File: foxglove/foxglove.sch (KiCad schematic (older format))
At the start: 23 parts, among them J1 NEIGHBOR1, J2 NEIGHBOR2, J7 BONUS_ROW, U10 iCE40HX4K

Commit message: Added iCE40-HX8K-CT256 to schematic, began signal routing.
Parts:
- removed C? (x2): 100nF, symbol Device:C
- removed C? (x2): 10uF, symbol Device:C
- removed J?: Conn_01x02, symbol Connector_Generic:Conn_01x02
- removed R? (x2): 100, symbol Device:R
- removed R? (x3): 10k, symbol Device:R
- removed U10: iCE40HX4K, gsg-modules:LQFP144, symbol gsg-symbols:iCE40HX4K
- removed U? (x5): ICE40HX8K-BG121, Package_BGA:BGA-121_9.0x9.0mm_Layout11x11_P0.8mm_Ball0.4mm_Pad0.35mm_NSMD, symbol FPGA_Lattice:ICE40HX8K-BG121
- added C? (x2): 10uF, symbol Device:C
- added C? (x2): 100nF, symbol Device:C
- added R? (x2): 100, symbol Device:R
- added R? (x3): 10k, symbol Device:R
- added R?: ???, symbol Device:R
- added U1: ICE40HX8K-CT256, BGA256C80P16X16_1400X1400X170, symbol gsg-symbols:ICE40HX8K-CT256
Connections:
- net labels added: J1.03, J1.04, J1.05, J1.06, J1.07, J1.08, J1.09, J1.10, J1.11, J1.12, J1.13, J1.14, J1.15, J1.16, J1.17, J1.18, J1.19, J1.20, J1.21, J1.22, J1.23, J1.24, J1.25, J1.26, J1.27, J1.28, J1.29, J1.30, J1.31, J1.32, J1.33, J1.34, J1.35, J1.36
- net labels removed: SPI_MISO, SPI_MOSI, SPI_SCK, SPI_SSEL
- wire segments 96 -> 57
- no-connect marks 65 -> 59
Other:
- note added: "add picture?\n"
- note removed: "FPGA should be able to reroute all GreatFET pins"
- note removed: "P0_0"
- note removed: "P0_1"
- note removed: "P1_0"
- note removed: "P1_10"
- note removed: "P1_11"
- note removed: "P1_12"
- note removed: "P1_13"
- note removed: "P1_14"
- note removed: "P1_15"
- note removed: "P1_16"
- note removed: "P1_7"
- note removed: "P1_8"
- note removed: "P1_9"
- note removed: "P5_0"
- note removed: "P5_1"
- note removed: "don't connect PLL ground\nto board ground"
- moved on the sheet: J1, J2, J7, MH1, MH2, MH3, MH4

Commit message: Foxglove: Routed signals to FPGA and set up bank A multiplexors
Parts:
- added C10, C11, C12, C5, C6, C7: 1uF, gsg-modules:0402, symbol Device:C
- added C8, C9: 0.1uF, gsg-modules:0402, symbol Device:C
- added J3, J4: Conn_02x05_Odd_Even, gsg-modules:HEADER-2x5, symbol Connector_Generic:Conn_02x05_Odd_Even
- added J5: Conn_01x02_Female, gsg-modules:HEADER-1x2, symbol Connector_Generic:Conn_01x02
- added R10, R15, R7: 10k, gsg-modules:0402, symbol Device:R
- added R11, R14: 165k, gsg-modules:0402, symbol Device:R
- added R12, R16: 20k, gsg-modules:0402, symbol Device:R
- added R13, R8: 217k, gsg-modules:0402, symbol Device:R
- added R9: 5k, gsg-modules:0402, symbol Device:R
- added U2: TLV711, Package_SON:WSON-6_1.5x1.5mm_P0.5mm, symbol gsg-symbols:TLV711
- added U3: MC4558CPT, Package_SO:TSSOP-8_4.4x3mm_P0.65mm, symbol gsg-symbols:MC4558CPT
- added U4: 74LVC1G3157, gsg-modules:SOT363, symbol gsg-symbols:74LVC1G3157
- added U5: LM339, Package_SO:SOIC-14_3.9x8.7mm_P1.27mm, symbol gsg-symbols:LM339
- added U6: ADP225, Package_CSP:LFCSP-8_2x2mm_P0.5mm, symbol gsg-symbols:ADP225
- added U7: DAC084S085, Package_SON:WSON-8-1EP_3x3mm_P0.5mm_EP1.6x2.0mm, symbol gsg-symbols:DAC084S085
- added U8: 74AHC1G04, Package_TO_SOT_SMD:SOT-886, symbol gsg-symbols:74AHC1G04
- C1, C2, C3, C4: renamed from C?; footprint (none) -> gsg-modules:0402
- R1, R2, R3, R4, R5, R6: renamed from R?; footprint (none) -> gsg-modules:0402
- U1: footprint BGA256C80P16X16_1400X1400X170 -> gsg-modules:BGA256C80P16X16_1400X1400X170
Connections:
- net +1V2: now also C7.1, U2.6 (OUT1)
- net +2V5: now also C6.1, U2.5 (OUT2)
- net +5V: now also C11.1, C5.1, C8.1, C9.2, R15.1, U2.1 (EN1), U2.2 (IN), U2.3 (EN2), U3.8 (VCC+), U5.3 (VCC), U6.6 (VIN), U7.7 (VREFIN)
- net GND: now also C10.2, C11.2, C12.2, C5.2, C6.2, C7.2, C8.2, C9.1, J3.10 (Pin_10), J4.10 (Pin_10), J5.1 (Pin_1), R10.1, R12.1, R16.2, R7.2, U2.4 (GND), U3.4 (VCC-), U4.2 (GND), U5.12 (GND), U6.3 (GND), U7.6 (GND), U8.3 (GND)
- net J1.03: now also U1.P13 (IOB_104_CBSEL1); no longer U1.R16 (IOB_102)
- net J1.04: now also U1.K11 (IOB_103_CBSEL0); no longer U1.M12 (IOB_101)
- net J1.05: now also U1.R16 (IOB_102); no longer U1.T16 (IOB_100)
- net J1.06: now also U1.M12 (IOB_101); no longer U1.L11 (IOB_99)
- net J1.07: now also U1.T16 (IOB_100)
- net J1.08: now also U1.L11 (IOB_99)
- net J1.09: now also U1.N12 (IOB_98)
- net J1.10: now also U1.T13 (IOB_94)
- net J1.11: now also U1.M11 (IOB_93)
- net J1.12: now also U1.T14 (IOB_92)
- net J1.13: now also U1.T15 (IOB_91)
- net J1.14: now also U1.T11 (IOB_89)
- net J1.15: now also U1.T10 (IOB_88)
- net J1.16: now also U1.N10 (IOB_87)
- net J1.17: now also U1.P10 (IOB_86)
- net J1.18: now also U1.L10 (IOB_85)
- net J1.19: now also U1.R10 (IOB_84)
- net J1.20: now also U1.P9 (IOB_83)
- net J1.21: now also U1.K9 (IOB_82_GBIN4)
- net J1.22: now also U1.R9 (IOB_81_GBIN5)
- net J1.23: now also U1.M9 (IOB_80)
- net J1.24: now also U1.T9 (IOB_79)
- net J1.25: now also U1.N9 (IOB_78)
- net J1.26: now also U1.P7 (IOB_77)
- net J1.27: now also U1.T8 (IOB_76)
- net J1.28: now also U1.T7 (IOB_75)
- net J1.29: now also U1.L9 (IOB_74)
- net J1.30: now also U1.T6 (IOB_73)
- net J1.32: now also U1.P8 (IOB_72)
- net J1.33: now also U1.R6 (IOB_71)
- net J1.34: now also U1.T5 (IOB_69)
- net J1.35: now also U1.M8 (IOB_68)
- net J1.36: now also U1.P6 (IOB_67)
- net MOSI: now also U7.8 (DIN)
- net SCK: now also U7.10 (SCLK)
- net SSEL: now also U8.2 (A)
- net VCC: now also J4.9 (Pin_9), U4.5 (VCC), U8.6 (VCC); no longer U1.C15 (VCCIO_1), U1.E1 (VCCIO_3), U1.G6 (VCCIO_3), U1.H10 (VCCIO_1), U1.H15 (VCCIO_1), U1.J6 (VCCIO_3), U1.N1 (VCCIO_3), U1.N15 (VCCIO_1)
- net J2.10: now reaches J2.10 (Pin_10)
- net J2.10: now also U1.C9 (IOT_191)
- net J2.11: now reaches J2.11 (Pin_11)
- net J2.11: now also U1.E9 (IOT_192)
- net J2.12: now reaches J2.12 (Pin_12)
- net J2.12: now also U1.D9 (IOT_193)
- net J2.13: now reaches J2.13 (Pin_13)
- net J2.13: now also U1.A9 (IOT_194)
- net J2.14: now reaches J2.14 (Pin_14)
- net J2.14: now also U1.F9 (IOT_196)
- net J2.15: now reaches J2.15 (Pin_15)
- net J2.15: now also U1.C8 (IOT_197_GBIN1)
- net J2.16: now reaches J2.16 (Pin_16)
- net J2.16: now also U1.F7 (IOT_198_GBIN0)
- net J2.17: now reaches J2.17 (Pin_17)
- net J2.17: now also U1.B9 (IOT_199)
- net J2.18: now reaches J2.18 (Pin_18)
- net J2.18: now also U1.D8 (IOT_200)
- net J2.19: now reaches J2.19 (Pin_19)
- net J2.19: now also U1.B8 (IOT_203)
- net J2.20: now reaches J2.20 (Pin_20)
- net J2.20: now also U1.A7 (IOT_205)
- net J2.21: now reaches J2.21 (Pin_21)
- net J2.21: now also U1.C7 (IOT_206)
- net J2.22: now reaches J2.22 (Pin_22)
- net J2.22: now also U1.B7 (IOT_207)
- net J2.23: now reaches J2.23 (Pin_23)
- net J2.23: now also U1.B6 (IOT_208)
- net J2.24: now reaches J2.24 (Pin_24)
- net J2.24: now also U1.C6 (IOT_209)
- net J2.25: now reaches J2.25 (Pin_25)
- net J2.25: now also U1.D7 (IOT_210)
- net J2.26: now reaches J2.26 (Pin_26)
- net J2.26: now also U1.A6 (IOT_211)
- net J2.27: now reaches J2.27 (Pin_27)
- net J2.27: now also U1.D6 (IOT_212)
- net J2.28: now reaches J2.28 (Pin_28)
- net J2.28: now also U1.A5 (IOT_213)
- net J2.29: now reaches J2.29 (Pin_29)
- net J2.29: now also U1.B5 (IOT_214)
- net J2.03: now reaches J2.3 (Pin_3)
- net J2.03: now also U1.B12 (IOT_182)
- net J2.30: now reaches J2.30 (Pin_30)
- net J2.30: now also U1.E6 (IOT_215)
- net J2.31: now reaches J2.31 (Pin_31)
- net J2.31: now also U1.B4 (IOT_216)
- net J2.32: now reaches J2.32 (Pin_32)
- net J2.32: now also U1.A2 (IOT_218)
- net J2.33: now reaches J2.33 (Pin_33)
- net J2.33: now also U1.D5 (IOT_219)
- net J2.34: now reaches J2.34 (Pin_34)
- net J2.34: now also U1.A1 (IOT_220)
- net J2.35: now reaches J2.35 (Pin_35)
- net J2.35: now also U1.C4 (IOT_222)
- net J2.36: now reaches J2.36 (Pin_36)
- net J2.36: now also U1.B3 (IOT_223)
- net J2.37: now reaches J2.37 (Pin_37)
- net J2.37: now also U1.D4 (IOT_224)
- net J2.38: now reaches J2.38 (Pin_38)
- net J2.38: now also U1.E5 (IOT_225)
- net J2.39: now reaches J2.39 (Pin_39)
- net J2.39: now also U1.D3 (IOT_226)
- net J2.04: now reaches J2.4 (Pin_4)
- net J2.04: now also U1.B10 (IOT_183)
- net J2.40: now reaches J2.40 (Pin_40)
- net J2.40: now also U1.C3 (IOT_227)
- net ADC: now reaches J2.5 (Pin_5)
- net ADC: now also R10.2, R9.2, U4.1 (B1)
- net J2.06: now reaches J2.6 (Pin_6)
- net J2.06: now also U1.C10 (IOT_185)
- net J2.07: now reaches J2.7 (Pin_7)
- net J2.07: now also U1.A10 (IOT_186)
- net J2.08: now reaches J2.8 (Pin_8)
- net J2.08: now also U1.A11 (IOT_187)
- net J2.09: now reaches J2.9 (Pin_9)
- net J2.09: now also U1.D10 (IOT_190)
- net B8: now reaches U1.A16 (IOT_176)
- net B8: now also J4.8 (Pin_8)
- net B4: now reaches U1.B14 (IOT_171)
- net B4: now also J4.4 (Pin_4)
- net B2: now reaches U1.B15 (IOT_169)
- net B2: now also J4.2 (Pin_2)
- net B5: now reaches U1.C12 (IOT_172)
- net B5: now also J4.5 (Pin_5)
- net B7: now reaches U1.C13 (IOT_174)
- net B7: now also J4.7 (Pin_7)
- net B1: now reaches U1.C14 (IOT_168)
- net B1: now also J4.1 (Pin_1)
- net B3: now reaches U1.D13 (IOT_170)
- net B3: now also J4.3 (Pin_3)
- net B6: now reaches U1.E11 (IOT_173)
- net B6: now also J4.6 (Pin_6)
- net A8_shift: now reaches U1.B16 (IOR_165)
- net ~E~_8: now reaches U1.C16 (IOR_161)
- net S0_8: now reaches U1.D15 (IOR_157)
- net S2_7: now reaches U1.D16 (IOR_153)
- net S2_8: now reaches U1.E14 (IOR_160)
- net S0_7: now reaches U1.E16 (IOR_151)
- net S1_8: now reaches U1.F11 (IOR_158)
- net A7_shift: now reaches U1.F12 (IOR_156)
- net DIR_8: now reaches U1.F13 (IOR_162)
- net DIR_7: now reaches U1.F14 (IOR_155)
- net DIR_6: now reaches U1.F15 (IOR_149)
- net S2_6: now reaches U1.F16 (IOR_147)
- net S1_6: now reaches U1.G10 (IOR_146)
- net ~E~_6: now reaches U1.G11 (IOR_148)
- net ~E~_7: now reaches U1.G12 (IOR_154)
- net S1_7: now reaches U1.G13 (IOR_152)
- net A6_shift: now reaches U1.G14 (IOR_150)
- net S0_6: now reaches U1.G15 (IOR_145)
- net DIR_5: now reaches U1.G16 (IOR_143)
- net A5_shift: now reaches U1.H12 (IOR_144)
- net S2_5: now reaches U1.H13 (IOR_139)
- net ~E~_5: now reaches U1.H14 (IOR_142)
- net S1_3: now reaches U1.J10 (IOR_122)
- net ~E~_3: now reaches U1.J11 (IOR_126)
- net A4_shift: now reaches U1.J12 (IOR_136)
- net S0_5: now reaches U1.J13 (IOR_137)
- net DIR_4: now reaches U1.J14 (IOR_134)
- net S1_4: now reaches U1.J15 (IOR_130)
- net S1_5: now reaches U1.J16 (IOR_138)
- net A2_shift: now reaches U1.K12 (IOR_120)
- net A3_shift: now reaches U1.K13 (IOR_128)
- net S0_4: now reaches U1.K14 (IOR_129)
- net S2_4: now reaches U1.K15 (IOR_131)
- net ~E~_4: now reaches U1.K16 (IOR_133)
- net S1_2: now reaches U1.L12 (IOR_116)
- net ~E~_2: now reaches U1.L13 (IOR_118)
- net DIR_2: now reaches U1.L14 (IOR_119)
- net DIR_3: now reaches U1.L16 (IOR_127)
- net A1_shift: now reaches U1.M13 (IOR_114)
- net S0_2: now reaches U1.M14 (IOR_115)
- net S2_3: now reaches U1.M15 (IOR_123)
- net S0_3: now reaches U1.M16 (IOR_121)
- net S2_2: now reaches U1.N16 (IOR_117)
- net S2_1: now reaches U1.P14 (IOR_111)
- net ~E~_1: now reaches U1.P15 (IOR_112)
- net DIR_1: now reaches U1.P16 (IOR_113)
- net S0_1: now reaches U1.R14 (IOR_109)
- net S1_1: now reaches U1.R15 (IOR_110)
- net COUT4: now reaches U1.N6 (IOB_52)
- net COUT4: now also U5.13 (4OUT)
- net COUT2: now reaches U1.P4 (IOB_54)
- net COUT2: now also U5.2 (2OUT)
- net VCCA_EN: now reaches U1.P5 (IOB_58)
- net VCCA_EN: now also U6.1 (EN1)
- net COUT1: now reaches U1.R2 (IOB_55)
- net COUT1: now also U5.1 (1OUT)
- net COUT3: now reaches U1.T1 (IOB_53)
- net COUT3: now also U5.14 (3OUT)
- net DAC2_EN: now reaches U1.T2 (IOB_57)
- net DAC2_EN: now also U6.2 (EN2)
- new net: U1.C15 (VCCIO_1), U1.H10 (VCCIO_1), U1.H15 (VCCIO_1), U1.N15 (VCCIO_1)
- new net: U1.E1 (VCCIO_3), U1.G6 (VCCIO_3), U1.J6 (VCCIO_3), U1.N1 (VCCIO_3)
- new net: R9.1, U4.3 (B0)
- new net: R7.1, U4.6 (SEL)
- new net: R15.2, U7.9 (~SYNC~), U8.4 (Y)
- new net: R11.2, R12.2, R8.1, U6.4 (ADJ2)
- new net: R13.2, R14.2, R16.1, U6.8 (ADJ1)
- new net A1: J3.1 (Pin_1)
- new net A2: J3.2 (Pin_2)
- new net A3: J3.3 (Pin_3)
- new net A4: J3.4 (Pin_4)
- new net A5: J3.5 (Pin_5)
- new net A6: J3.6 (Pin_6)
- new net A7: J3.7 (Pin_7)
- new net A8: J3.8 (Pin_8)
- new net ADC_A: U4.4 (A)
- new net COMP1: U5.5 (2IN+), U5.6 (1IN-), U5.9 (3IN+)
- new net COMP2: U5.11 (4IN+), U5.7 (1IN+)
- new net DAC2: C10.1, R11.1, U5.4 (2IN-), U6.5 (VOUT2)
- new net DAC3: U3.1 (O1), U3.2 (I1-), U5.8 (3IN-)
- new net DAC4: U3.6 (I2-), U3.7 (O2), U5.10 (4IN-)
- new net VCCA: C12.1, J3.9 (Pin_9), J5.2 (Pin_2), R14.1, U6.7 (VOUT1)
- no-connect marks 59 -> 21
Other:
- note added: "add another LDO\nfor DAC3 and DAC4?"
- note added: "add ext clipper?"
- note added: "bank A: ADC, DAC, level shifter, pull-up, pull-down, comparator\nbank B: FPGA"
- note added: "check digital levels\nfor comp (5V)"
- note added: "check digital levels\nfor mux (5V)"
- note added: "comparator bank"
- note added: "optional external \nsupply input"
- note removed: "add picture?\n"
- moved on the sheet: J1, J2, J7, R1, R2, R4, R5, U1A, U1B, U1C, U1D

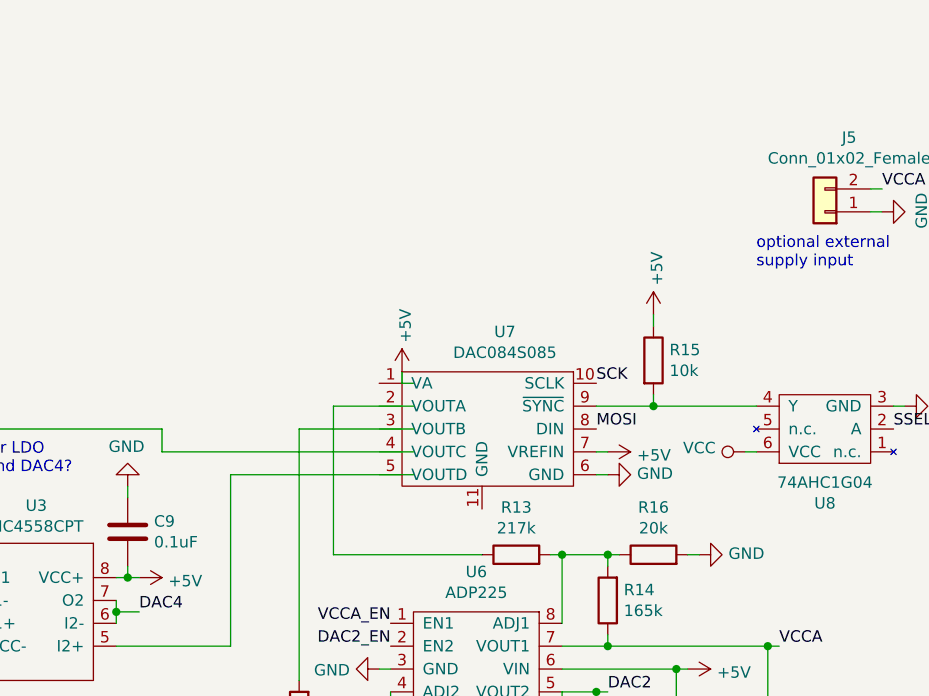
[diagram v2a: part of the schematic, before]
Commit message: Continued work on Foxglove schematic (added bypass caps, selected footprints, etc.). Placed parts on PCB.
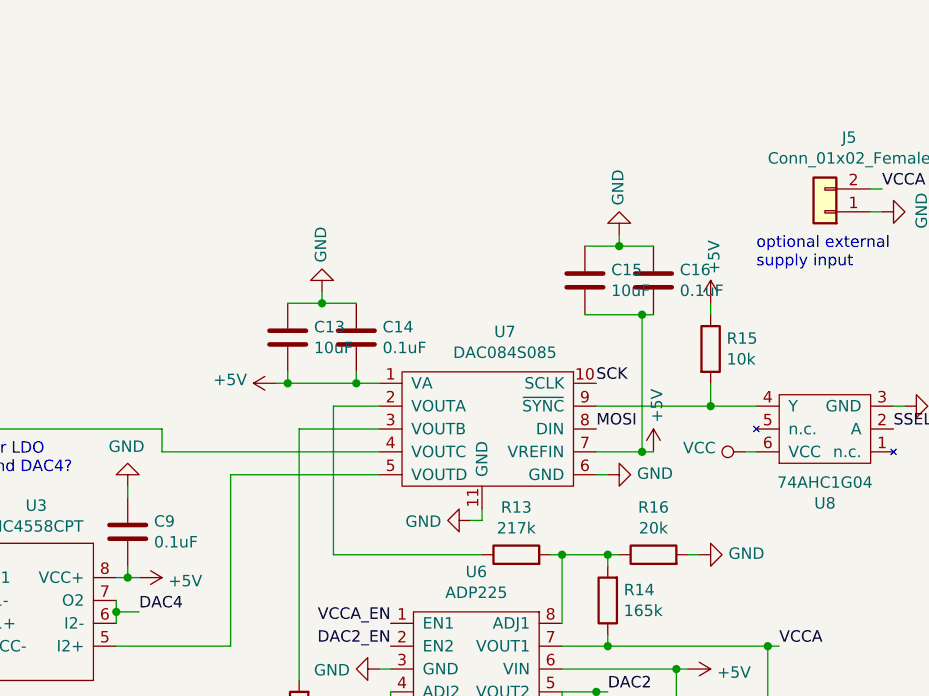
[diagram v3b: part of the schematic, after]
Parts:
- added C13, C15: 10uF, Capacitor_SMD:C_1206_3216Metric, symbol Device:C
- added C14, C16: 0.1uF, gsg-modules:0805, symbol Device:C
- U4: Description (none) -> IC SWITCH SPDT 6 OHM SOT363; Manufacturer (none) -> Diodes Incorporated; Part Number (none) -> 74LVC1G3157DW-7
- U7: footprint Package_SON:WSON-8-1EP_3x3mm_P0.5mm_EP1.6x2.0mm -> Package_SON:WSON-10-1EP_4x3mm_P0.5mm_EP2.2x2mm
- U8: Description (none) -> IC INVERTER 1CH 1-INP SOT23-5; Manufacturer (none) -> Texas Instruments; Part Number (none) -> SN74AHC1G04QDBVRQ1
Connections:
- net +5V: now also U7.1 (VA), C13.1, C14.2, C15.1, C16.2
- net GND: now also U7.11 (GND), C13.2, C14.1, C15.2, C16.1
- net at U3.3 (I1+): now also U7.4 (VOUTC)
- net at U3.5 (I2+): now also U7.5 (VOUTD)
- net at U7.2 (VOUTA): now also R13.1
- net at U7.3 (VOUTB): now also R8.2
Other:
- moved on the sheet: R15
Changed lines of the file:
@@
 F 2 "gsg-modules:SOT363" H 13050 1850 50  0001 C CNN
 F 3 "" H 13050 1850 50  0001 C CNN
+F 4 "Diodes Incorporated " H 13050 1850 50  0001 C CNN "Manufacturer"
+F 5 "74LVC1G3157DW-7 " H 13050 1850 50  0001 C CNN "Part Number"
+F 6 "IC SWITCH SPDT 6 OHM SOT363 " H 13050 1850 50  0001 C CNN "Description"
 	1    13050 1850
 	-1   0    0    1
@@
 F 0 "U7" H 14450 7825 50  0000 C CNN
 F 1 "DAC084S085" H 14450 7734 50  0000 C CNN
-F 2 "Package_SON:WSON-8-1EP_3x3mm_P0.5mm_EP1.6x2.0mm" H 14350 7500 50  0001 C CNN
+F 2 "Package_SON:WSON-10-1EP_4x3mm_P0.5mm_EP2.2x2mm" H 14350 7500 50  0001 C CNN
 F 3 "" H 14350 7500 50  0001 C CNN
 F 4 "Texas Instruments" H 14450 7400 50  0001 C CNN "Manufacturer"
@@
 L power:+5V #PWR?
 U 1 1 5D7BE9E7
-P 14000 7150
+P 13450 7200
 AR Path="/5C842523/5D7BE9E7" Ref="#PWR?"  Part="1"
 AR Path="/5D7BE9E7" Ref="#PWR0132"  Part="1"
-F 0 "#PWR0132" H 14000 7000 50  0001 C CNN
-F 1 "+5V" V 14015 7278 50  0000 L CNN
-F 2 "" H 14000 7150 50  0001 C CNN
-F 3 "" H 14000 7150 50  0001 C CNN
-	1    14000 7150
-	1    0    0    -1
-$EndComp
-Wire Wire Line
-	14000 7150 14000 7200
-Wire Wire Line
-	14000 7200 14050 7200
+F 0 "#PWR0132" H 13450 7050 50  0001 C CNN
+F 1 "+5V" V 13465 7328 50  0000 L CNN
+F 2 "" H 13450 7200 50  0001 C CNN
+F 3 "" H 13450 7200 50  0001 C CNN
+	1    13450 7200
+	0    -1   -1   0
+$EndComp
 $Comp
 L Device:R R?
 U 1 1 5D7BE9F0
-P 15100 7100
+P 15350 7050
 AR Path="/5C842523/5D7BE9F0" Ref="R?"  Part="1"
 AR Path="/5D7BE9F0" Ref="R15"  Part="1"
-F 0 "R15" H 15170 7146 50  0000 L CNN
-F 1 "10k" H 15170 7055 50  0000 L CNN
-F 2 "gsg-modules:0402" V 15030 7100 50  0001 C CNN
-F 3 "~" H 15100 7100 50  0001 C CNN
-	1    15100 7100
+F 0 "R15" H 15420 7096 50  0000 L CNN
+F 1 "10k" H 15420 7005 50  0000 L CNN
+F 2 "gsg-modules:0402" V 15280 7050 50  0001 C CNN
+F 3 "~" H 15350 7050 50  0001 C CNN
+	1    15350 7050
 	1    0    0    -1
 $EndComp
@@
 L power:+5V #PWR?
 U 1 1 5D7BE9FA
-P 15100 6900
+P 15350 6850
 AR Path="/5C842523/5D7BE9FA" Ref="#PWR?"  Part="1"
 AR Path="/5D7BE9FA" Ref="#PWR0133"  Part="1"
-F 0 "#PWR0133" H 15100 6750 50  0001 C CNN
-F 1 "+5V" V 15115 7028 50  0000 L CNN
-F 2 "" H 15100 6900 50  0001 C CNN
-F 3 "" H 15100 6900 50  0001 C CNN
-	1    15100 6900
-	1    0    0    -1
-$EndComp
-Wire Wire Line
-	14850 7500 14900 7500
+F 0 "#PWR0133" H 15350 6700 50  0001 C CNN
+F 1 "+5V" V 15365 6978 50  0000 L CNN
+F 2 "" H 15350 6850 50  0001 C CNN
+F 3 "" H 15350 6850 50  0001 C CNN
+	1    15350 6850
+	1    0    0    -1
+$EndComp
 $Comp
 L power:GND #PWR?
@@
 L power:+5V #PWR?
 U 1 1 5D7BEA27
-P 14900 7500
+P 15100 7500
 AR Path="/5C842523/5D7BEA27" Ref="#PWR?"  Part="1"
 AR Path="/5D7BEA27" Ref="#PWR0136"  Part="1"
-F 0 "#PWR0136" H 14900 7350 50  0001 C CNN
-F 1 "+5V" V 14915 7628 50  0000 L CNN
-F 2 "" H 14900 7500 50  0001 C CNN
-F 3 "" H 14900 7500 50  0001 C CNN
-	1    14900 7500
-	0    1    1    0
+F 0 "#PWR0136" H 15100 7350 50  0001 C CNN
+F 1 "+5V" V 15115 7628 50  0000 L CNN
+F 2 "" H 15100 7500 50  0001 C CNN
+F 3 "" H 15100 7500 50  0001 C CNN
+	1    15100 7500
+	1    0    0    -1
 $EndComp
 Wire Wire Line
@@
 $EndComp
 Wire Wire Line
-	14050 7300 13700 7300
-Wire Wire Line
 	13700 7300 13700 7950
 Wire Wire Line
@@
 $EndComp
 Wire Wire Line
-	14050 7400 13550 7400
-Wire Wire Line
 	13550 7400 13550 8500
 Wire Wire Line
@@
 Wire Wire Line
 	13550 8850 13950 8850
-Wire Wire Line
-	12950 7500 14050 7500
-Wire Wire Line
-	13250 7600 14050 7600
 Text Notes 11850 7600 0    50   ~ 0
 add another LDO\nfor DAC3 and DAC4?
@@
 U 1 1 5DD34267
 P 15850 7400
+AR Path="/5DD34267" Ref="U8"  Part="1"
+AR Path="/5CF421CD/5DD34267" Ref="U8"  Part="1"
 F 0 "U8" H 15850 7725 50  0000 C CNN
 F 1 "74AHC1G04" H 15850 7634 50  0000 C CNN
 F 2 "Package_TO_SOT_SMD:SOT-886" H 16050 7350 50  0001 C CNN
 F 3 "" H 16050 7350 50  0001 C CNN
+F 4 "Texas Instruments" H 15850 7400 50  0001 C CNN "Manufacturer"
+F 5 "SN74AHC1G04QDBVRQ1" H 15850 7400 50  0001 C CNN "Part Number"
+F 6 " IC INVERTER 1CH 1-INP SOT23-5 " H 15850 7400 50  0001 C CNN "Description"
 	1    15850 7400
 	-1   0    0    1
@@
 SSEL
 Wire Wire Line
-	14850 7300 15100 7300
-Wire Wire Line
-	15100 6900 15100 6950
-Wire Wire Line
-	15100 7250 15100 7300
-Connection ~ 15100 7300
-Wire Wire Line
-	15100 7300 15550 7300
+	15350 6850 15350 6900
 Wire Wire Line
 	1900 8950 1900 9150
 Wire Wire Line
 	1900 9150 1900 9450
+$Comp
+L Device:C C13
+U 1 1 5CA1CB44
+P 13500 7000
+F 0 "C13" H 13385 6954 50  0000 R CNN
+F 1 "10uF" H 13385 7045 50  0000 R CNN
+F 2 "Capacitor_SMD:C_1206_3216Metric" H 13538 6850 50  0001 C CNN
+F 3 "~" H 13500 7000 50  0001 C CNN
+F 4 "AVX Corporation" H 13500 7000 50  0001 C CNN "Manufacturer"
+F 5 "TAJA106K010TNJ" H 13500 7000 50  0001 C CNN "Part Number"
+F 6 "CAP TANT 10UF 10% 10V 1206 " H 13500 7000 50  0001 C CNN "Description"
+	1    13500 7000
+	-1   0    0    1
+$EndComp
+Wire Wire Line
+	13700 7300 13900 7300
+Wire Wire Line
+	13550 7400 13900 7400
+Wire Wire Line
+	12950 7500 13900 7500
+Wire Wire Line
+	13250 7600 13900 7600
+$Comp
+L power:GND #PWR?
+U 1 1 5CA86F7A
+P 14300 7800
+AR Path="/5C842523/5CA86F7A" Ref="#PWR?"  Part="1"
+AR Path="/5CA86F7A" Ref="#PWR0192"  Part="1"
+F 0 "#PWR0192" H 14300 7550 50  0001 C CNN
+F 1 "GND" V 14305 7672 50  0000 R CNN
+F 2 "" H 14300 7800 50  0001 C CNN
+F 3 "" H 14300 7800 50  0001 C CNN
+	1    14300 7800
+	0    1    1    0
+$EndComp
+Wire Wire Line
+	14350 7750 14350 7800
+Wire Wire Line
+	14350 7800 14300 7800
+$Comp
+L Device:C C14
+U 1 1 5CAA1802
+P 13800 7000
+F 0 "C14" H 13915 7046 50  0000 L CNN
+F 1 "0.1uF" H 13915 6955 50  0000 L CNN
+F 2 "gsg-modules:0805" H 13838 6850 50  0001 C CNN
+F 3 "~" H 13800 7000 50  0001 C CNN
+F 4 "Murata Electronics North America" H 13800 7000 50  0001 C CNN "Manufacturer"
+F 5 "LLL216R71E104MA01L" H 13800 7000 50  0001 C CNN "Part Number"
+F 6 "CAP CER 0.1UF 25V X7R 0508 " H 13800 7000 50  0001 C CNN "Description"
+	1    13800 7000
+	1    0    0    -1
+$EndComp
+Wire Wire Line
+	13450 7200 13500 7200
+Wire Wire Line
+	13500 7200 13500 7150
+Wire Wire Line
+	13500 7200 13800 7200
+Wire Wire Line
+	13800 7200 13800 7150
+Connection ~ 13500 7200
+Wire Wire Line
+	13800 7200 13900 7200
+Connection ~ 13800 7200
+Wire Wire Line
+	13500 6850 13650 6850
+Wire Wire Line
+	13650 6850 13650 6800
+Connection ~ 13650 6850
+Wire Wire Line
+	13650 6850 13800 6850
+$Comp
+L power:GND #PWR?
+U 1 1 5CB2834B
+P 13650 6800
+AR Path="/5C842523/5CB2834B" Ref="#PWR?"  Part="1"
+AR Path="/5CB2834B" Ref="#PWR0193"  Part="1"
+F 0 "#PWR0193" H 13650 6550 50  0001 C CNN
+F 1 "GND" V 13655 6672 50  0000 R CNN
+F 2 "" H 13650 6800 50  0001 C CNN
+F 3 "" H 13650 6800 50  0001 C CNN
+	1    13650 6800
+	-1   0    0    1
+$EndComp
+$Comp
+L Device:C C15
+U 1 1 5CB5F3F3
+P 14800 6750
+F 0 "C15" H 14685 6704 50  0000 R CNN
+F 1 "10uF" H 14685 6795 50  0000 R CNN
+F 2 "Capacitor_SMD:C_1206_3216Metric" H 14838 6600 50  0001 C CNN
+F 3 "~" H 14800 6750 50  0001 C CNN
+F 4 "AVX Corporation" H 14800 6750 50  0001 C CNN "Manufacturer"
+F 5 "TAJA106K010TNJ" H 14800 6750 50  0001 C CNN "Part Number"
+F 6 "CAP TANT 10UF 10% 10V 1206 " H 14800 6750 50  0001 C CNN "Description"
+	1    14800 6750
+	-1   0    0    1
+$EndComp
+$Comp
+L Device:C C16
+U 1 1 5CB5F3FD
+P 15100 6750
+F 0 "C16" H 15215 6796 50  0000 L CNN
+F 1 "0.1uF" H 15215 6705 50  0000 L CNN
+F 2 "gsg-modules:0805" H 15138 6600 50  0001 C CNN
+F 3 "~" H 15100 6750 50  0001 C CNN
+F 4 "Murata Electronics North America" H 15100 6750 50  0001 C CNN "Manufacturer"
+F 5 "LLL216R71E104MA01L" H 15100 6750 50  0001 C CNN "Part Number"
+F 6 "CAP CER 0.1UF 25V X7R 0508 " H 15100 6750 50  0001 C CNN "Description"
+	1    15100 6750
+	1    0    0    -1
+$EndComp
+Wire Wire Line
+	14800 6600 14950 6600
+Wire Wire Line
+	14950 6600 14950 6550
+Connection ~ 14950 6600
+Wire Wire Line
+	14950 6600 15100 6600
+$Comp
+L power:GND #PWR?
+U 1 1 5CB5F408
+P 14950 6550
+AR Path="/5C842523/5CB5F408" Ref="#PWR?"  Part="1"
+AR Path="/5CB5F408" Ref="#PWR0194"  Part="1"
+F 0 "#PWR0194" H 14950 6300 50  0001 C CNN
+F 1 "GND" V 14955 6422 50  0000 R CNN
+F 2 "" H 14950 6550 50  0001 C CNN
+F 3 "" H 14950 6550 50  0001 C CNN
+	1    14950 6550
+	-1   0    0    1
+$EndComp
+Wire Wire Line
+	14850 7300 15350 7300
+Wire Wire Line
+	15350 7200 15350 7300
+Connection ~ 15350 7300
+Wire Wire Line
+	15350 7300 15550 7300
+Wire Wire Line
+	14800 6900 15050 6900
+Wire Wire Line
+	15050 6900 15050 7500
+Wire Wire Line
+	14850 7500 15050 7500
+Connection ~ 15050 6900
+Wire Wire Line
+	15050 6900 15100 6900
+Wire Wire Line
+	15100 7500 15050 7500
 Wire Bus Line
 	3900 1900 5900 1900
@@
 Wire Bus Line
 	3150 6800 6350 6800
+Connection ~ 15050 7500
 $EndSCHEMATC
